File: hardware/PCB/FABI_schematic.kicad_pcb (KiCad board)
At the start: 2 copper layers, 78 x 55 mm, 37 parts, among them J1 Cliff_68125, J10 Conn_01x03_Male, J11 Conn_01x04_Male, J11_disp1 Conn_01x04_Female, J2 Cliff_68125, J3 Cliff_68125, J4 Cliff_68125, J5 Cliff_68125, J6 Cliff_68125, J7 Cliff_68125, J8 Cliff_68125, J9 Conn_02x05_Odd_Even, U1 MPXV7007GP, U2 ProMicro

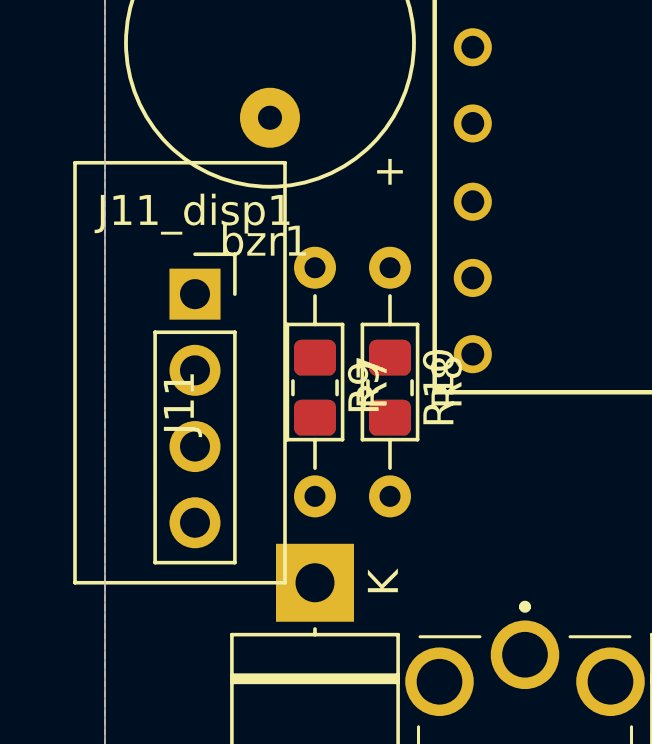
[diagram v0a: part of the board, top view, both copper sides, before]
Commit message: Pins changed and connected to AddOn
Signed-off-by: fussthalerandreas <fussthaler.andreas1997@gmail.com>
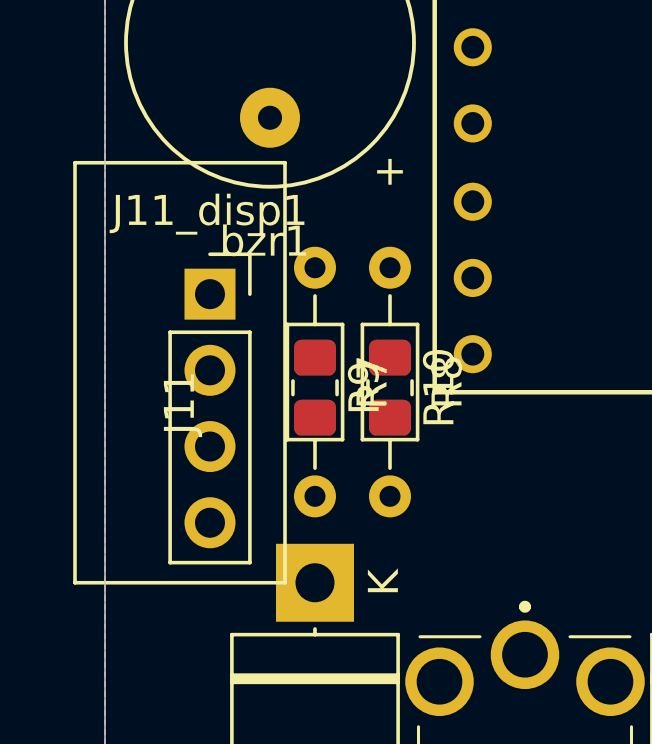
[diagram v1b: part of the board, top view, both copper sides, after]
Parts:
- moved J11_disp1 0.50 mm to (76.5, 124.4)

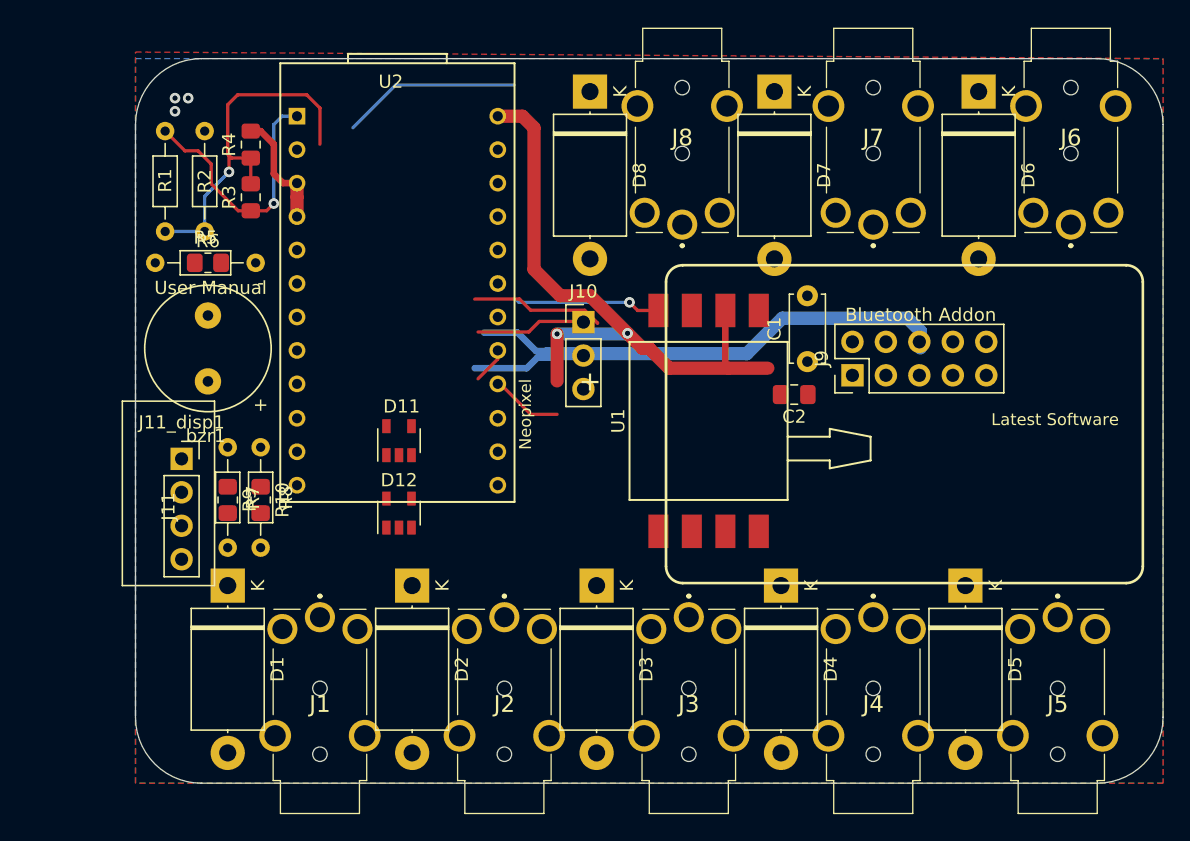
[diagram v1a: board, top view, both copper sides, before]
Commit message: Display positioning: adding adapted PinSocket to enable soldering and pluggin in of the display, 3D Models adapted
Signed-off-by: fussthalerandreas <fussthaler.andreas1997@gmail.com>
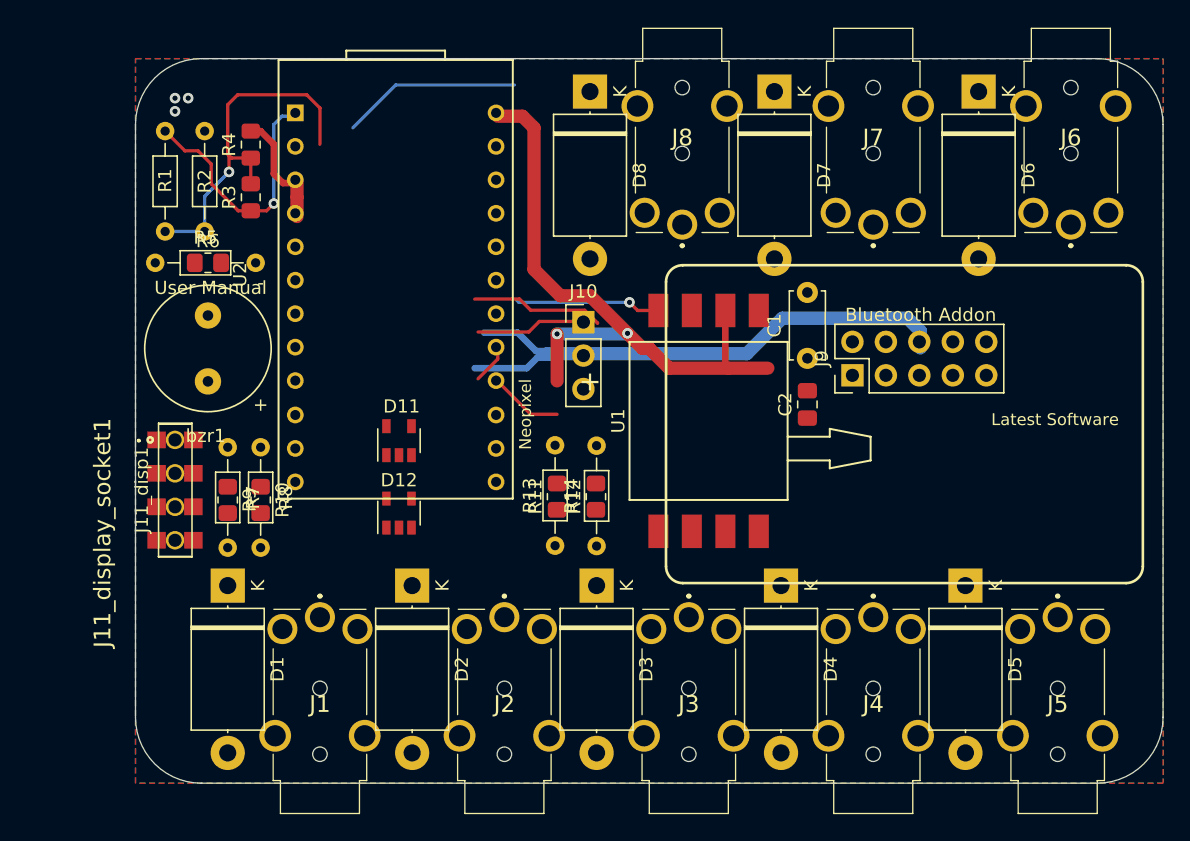
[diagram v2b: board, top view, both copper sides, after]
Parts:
- removed J11: Conn_01x04_Male, Connector:display
- added J11_display_socket1: 91601-304LF, SamacSys_Parts:91601304LF, F.Cu at (76.0, 126.8)
- added R11: 10k, Resistor_SMD:R_0805_2012Metric_Pad1.20x1.40mm_HandSolder, F.Cu at (105.0, 127.2)
- added R12: 18k, Resistor_SMD:R_0805_2012Metric_Pad1.20x1.40mm_HandSolder, F.Cu at (108.0, 127.2)
- added R13: 10k, Resistor_THT:R_Axial_DIN0204_L3.6mm_D1.6mm_P7.62mm_Horizontal, F.Cu at (104.8, 131.0)
- added R14: 18k, Resistor_THT:R_Axial_DIN0204_L3.6mm_D1.6mm_P7.62mm_Horizontal, F.Cu at (108.0, 131.0)
- J11_disp1: footprint Connector_PinSocket_2.54mm:PinSocket_1x04_P2.54mm_Vertical -> FABI_customLibs:OLED_display_091
- moved J11_disp1 2.95 mm to (74.8, 126.8), turned to 90 degrees
- moved C2 1.25 mm to (124.0, 120.2), turned to 90 degrees
- moved U2 0.28 mm to (92.8, 110.8)
- moved C1 0.25 mm to (124.0, 116.8)
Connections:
- net buzzer_pin renamed Buzzer_Pin
- J9 pad 1: AddOn_Pin1 -> ESP_AddOn_Pin1
- J9 pad 9: VCC -> VDD
- U2 pad 21: (no net) -> VCC
- U2 pad 24: VCC -> VDD
- U2 pad 5: SCL -> SDA
- U2 pad 6: SDA -> SCL

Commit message: Signed-off-by: fussthalerandreas <fussthaler.andreas1997@gmail.com>
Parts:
- removed J11_display_socket1: 91601-304LF, SamacSys_Parts:91601304LF
- added J11: dispaly_connector_91601-304LF, FABI_customLibs:91601304LF, F.Cu at (76.5, 126.2)
- moved R9 2.66 mm to (81.8, 125.5), turned to 0 degrees
- moved R7 0.90 mm to (80.5, 122.8)
- moved R8 0.79 mm to (82.8, 122.8)
- moved R10 0.75 mm to (81.8, 127.5), turned to 0 degrees
- moved J11_disp1 0.56 mm to (75.0, 126.2)
- moved D12 0.40 mm to (93.0, 128.9)
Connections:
- J1 pad 2R: (no net) -> Net-(J1-Pad2R)
- J1 pad 6SR: (no net) -> Net-(J1-Pad6SR)
- J2 pad 2R: (no net) -> Net-(J2-Pad2R)
- J2 pad 6SR: (no net) -> Net-(J2-Pad6SR)
- J3 pad 2R: (no net) -> Net-(J3-Pad2R)
- J3 pad 6SR: (no net) -> Net-(J3-Pad6SR)
- J4 pad 2R: (no net) -> Net-(J4-Pad2R)
- J4 pad 6SR: (no net) -> Net-(J4-Pad6SR)
- J5 pad 2R: (no net) -> Net-(J5-Pad2R)
- J5 pad 6SR: (no net) -> Net-(J5-Pad6SR)
- J6 pad 2R: (no net) -> Net-(J6-Pad2R)
- J6 pad 6SR: (no net) -> Net-(J6-Pad6SR)
- J7 pad 2R: (no net) -> Net-(J7-Pad2R)
- J7 pad 6SR: (no net) -> Net-(J7-Pad6SR)
- J8 pad 2R: (no net) -> Net-(J8-Pad2R)
- J8 pad 6SR: (no net) -> Net-(J8-Pad6SR)
- J9 pad 4: (no net) -> Net-(J9-Pad4)
- J9 pad 5: (no net) -> Net-(J9-Pad5)
- U1 pad 1: (no net) -> Net-(U1-Pad1)
- U1 pad 5: (no net) -> Net-(U1-Pad5)
- U1 pad 6: (no net) -> Net-(U1-Pad6)
- U1 pad 7: (no net) -> Net-(U1-Pad7)
- U1 pad 8: (no net) -> Net-(U1-Pad8)
- U2 pad 22: (no net) -> Net-(U2-Pad22)
- U2 pad 23: (no net) -> Net-(U2-Pad23)
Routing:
- net 5: track 0.00 -> 19.7 mm
- net 4: track 0.00 -> 19.7 mm
- net 3: track 0.00 -> 19.7 mm
- net 2: track 0.00 -> 19.7 mm
- net SDA: track 0.00 -> 17.4 mm
- net 1: track 0.00 -> 11.9 mm
- net SCL: track 0.00 -> 7.61 mm
- net Net-(R5-Pad2): track 0.00 -> 7.03 mm

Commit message: routed the PCB, adapted all components, ready for review
Signed-off-by: fussthalerandreas <fussthaler.andreas1997@gmail.com>
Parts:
- added REF**: ESP32_Addon, FABI_customLibs:ESP32_Addon, F.Cu at (132.5, 116.8)
- R3, R4: footprint Resistor_SMD:R_0805_2012Metric_Pad1.15x1.40mm_HandSolder -> Resistor_SMD:R_0805_2012Metric_Pad1.20x1.40mm_HandSolder
- U1: footprint MPXV7007:MPXV7007GP -> MPXV7007GP:MPXV7007GP
- moved R5 9.50 mm to (74.8, 119.0)
- moved R6 9.50 mm to (78.5, 119.0)
- moved R13 8.30 mm to (102.9, 122.9), turned to 0 degrees
- moved R14 7.50 mm to (102.9, 125.5), turned to 0 degrees
- moved D11 7.20 mm to (93.0, 130.2)
- moved D12 6.70 mm to (93.0, 122.2), turned to 0 degrees
- moved R4 5.13 mm to (78.5, 104.5), turned to 180 degrees
- moved R2 4.88 mm to (82.4, 104.5), turned to 180 degrees
- moved R11 4.67 mm to (106.7, 122.9), turned to 0 degrees
- moved bzr1 4.25 mm to (78.5, 111.8), turned to 0 degrees
- moved R3 3.97 mm to (78.5, 102.2), turned to 0 degrees
- moved R1 2.80 mm to (74.8, 102.2), turned to 0 degrees
- moved R7 2.25 mm to (82.8, 122.8)
- moved R12 2.15 mm to (106.7, 125.5), turned to 0 degrees
- moved R8 2.00 mm to (80.8, 122.8)
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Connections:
- U2 pad 10: 6 -> 3
- U2 pad 11: 1 -> 2
- U2 pad 12: 2 -> 1
- U2 pad 18: Buzzer_Pin -> 6
- U2 pad 7: 3 -> Buzzer_Pin
- U2 pad 8: 4 -> 5
- U2 pad 9: 5 -> 4
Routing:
- net 7: track 0.00 -> 69.3 mm, vias 0 -> 2
- net 6: track 13.8 -> 81.0 mm, vias 0 -> 1
- net 5: track 19.7 -> 79.4 mm
- net /A_RX: track 0.10 -> 58.8 mm, vias 0 -> 1
- net 8: track 0.00 -> 57.7 mm, vias 0 -> 2
- net VDD: track 0.00 -> 50.7 mm
- net 4: track 19.7 -> 64.1 mm
- net GND: track 52.2 -> 8.05 mm, vias 3 -> 0
- net VCC: track 56.2 -> 18.5 mm, vias 2 -> 0
- net /ESP_RX: track 37.8 -> 72.8 mm, vias 1 -> 2
- net AddOn_Pin3: track 0.00 -> 31.8 mm, vias 0 -> 1
- net 3: track 19.7 -> 50.8 mm
- net AddOn_Pin2: track 0.00 -> 29.0 mm
- net ESP_AddOn_Pin1: track 0.00 -> 28.2 mm
- net 1: track 11.9 -> 38.1 mm
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- added copper zone on B.Cu, net VCC
- removed copper zone on B.Cu, net GND

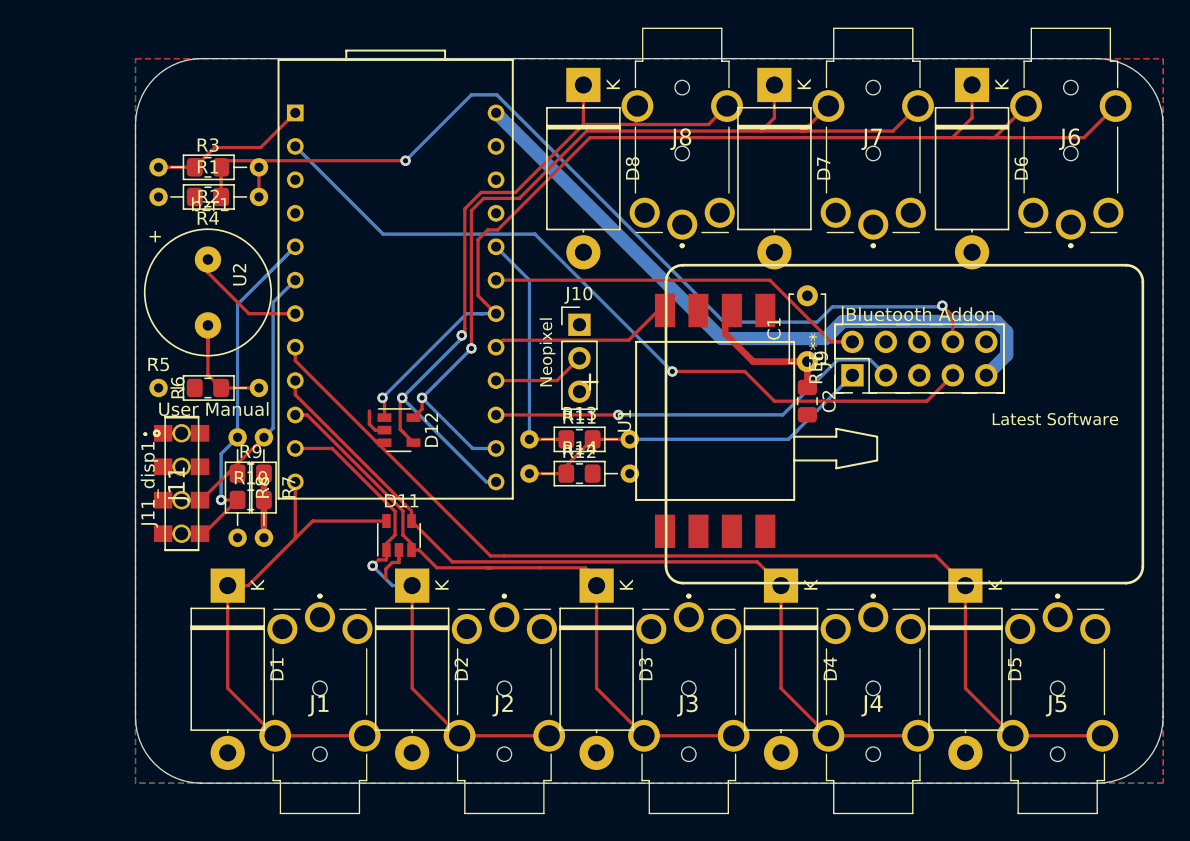
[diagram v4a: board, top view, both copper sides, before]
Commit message: PCB v2, after Feedback (according to Meeting 2)
Signed-off-by: fussthalerandreas <fussthaler.andreas1997@gmail.com>
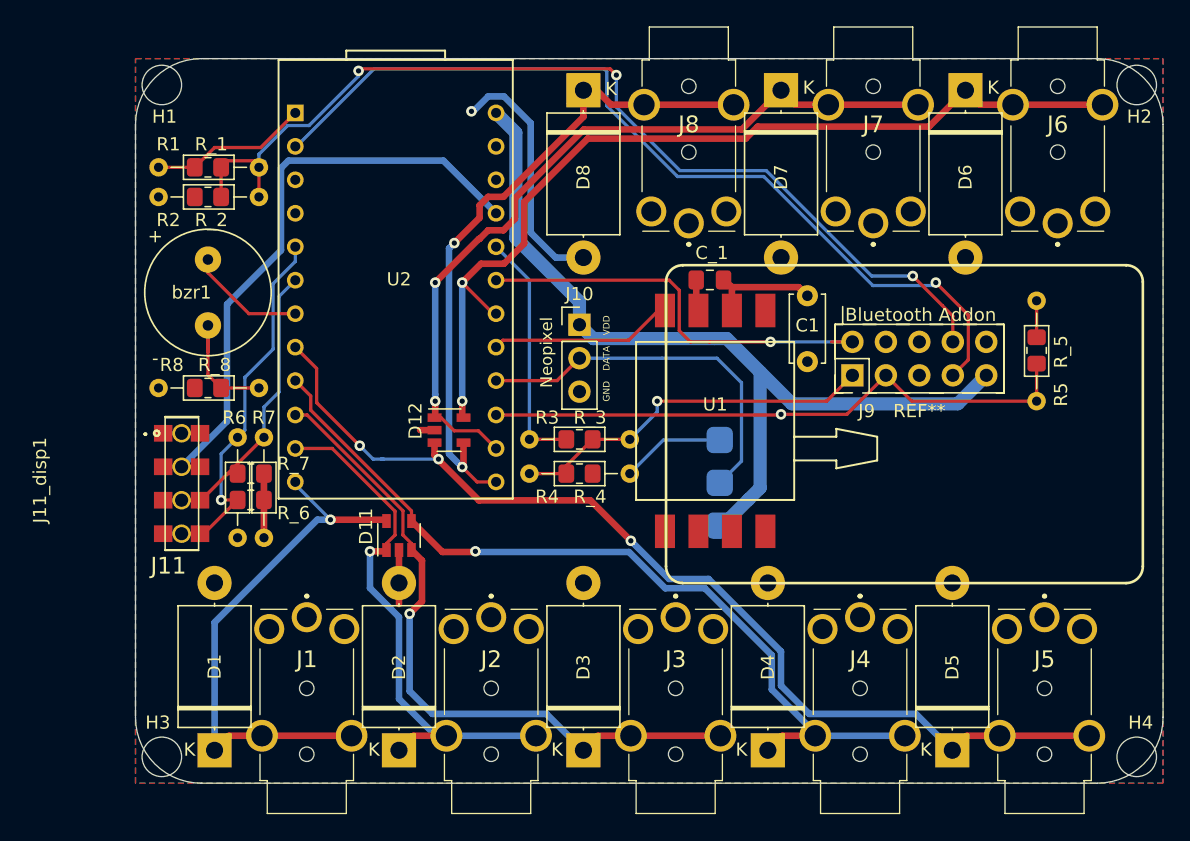
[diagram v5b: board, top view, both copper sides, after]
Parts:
- added DATA: SolderWirePad_1x01_SMD_1x2mm, Connector_Wire:SolderWirePad_1x01_SMD_1x2mm, B.Cu at (117.3, 126.2)
- added GND: SolderWirePad_1x01_SMD_1x2mm, Connector_Wire:SolderWirePad_1x01_SMD_1x2mm, B.Cu at (117.3, 123.0)
- added H1: MountingHole, MountingHole:MountingHole_3mm, F.Cu at (75.0, 96.0)
- added H2: MountingHole, MountingHole:MountingHole_3mm, F.Cu at (149.0, 96.0)
- added H3: MountingHole, MountingHole:MountingHole_3mm, F.Cu at (75.0, 147.0)
- added H4: MountingHole, MountingHole:MountingHole_3mm, F.Cu at (149.0, 147.0)
- added R5: 10k, Resistor_THT:R_Axial_DIN0204_L3.6mm_D1.6mm_P7.62mm_Horizontal, F.Cu at (141.4, 120.0)
- added R_5: 10k, Resistor_SMD:R_0805_2012Metric_Pad1.20x1.40mm_HandSolder, F.Cu at (141.4, 116.2)
- added VDD: SolderWirePad_1x01_SMD_1x2mm, Connector_Wire:SolderWirePad_1x01_SMD_1x2mm, B.Cu at (117.3, 129.4)
- moved D1 12.5 mm to (79.0, 146.5), turned to 90 degrees
- moved D2 12.5 mm to (93.0, 146.5), turned to 90 degrees
- moved D3 12.5 mm to (107.0, 146.5), turned to 90 degrees
- moved D4 12.5 mm to (121.0, 146.5), turned to 90 degrees
- moved D5 12.5 mm to (135.0, 146.5), turned to 90 degrees
- moved C_1 11.8 mm to (116.6, 110.8), turned to 180 degrees
- moved C1 5.00 mm to (124.0, 112.0), turned to 270 degrees
- moved D12 3.80 mm to (96.8, 122.2)
- moved J6 1.00 mm to (143.0, 99.9)
- moved J1 1.00 mm to (86.0, 143.0)
- moved J2 1.00 mm to (100.0, 143.0)
- moved J3 1.00 mm to (114.0, 143.0)
- moved J4 1.00 mm to (128.0, 143.0)
- moved J5 1.00 mm to (142.0, 143.0)
- moved D6 0.64 mm to (136.0, 96.4)
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- renumbered C2 to C_1, R13 to R3, R14 to R4, R8 to R6, R5 to R8, R3 to R_1, R4 to R_2, R11 to R_3, R12 to R_4, R10 to R_6, R9 to R_7, R6 to R_8
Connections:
- net /A_RX renamed A_RX
- net /A_TX renamed A_TX
- net /ESP_RX renamed ESP_RX
- net /MPX renamed MPX
- net /NEOPIXEL renamed NEOPIXEL
- net 1 renamed AUX_1
- net 2 renamed AUX_2
- net 3 renamed AUX_3
- net 4 renamed AUX_4
- net 5 renamed AUX_5
- net 8 renamed AUX_8
- D12 pad 1: 6 -> AUX_7
- D12 pad 5: 7 -> AUX_6
- D6 pad 1: 6 -> AUX_6
- D7 pad 1: 7 -> AUX_7
- J10 pad 1: VCC -> VDD
- J6 pad 3T: 6 -> AUX_6
- J7 pad 3T: 7 -> AUX_7
- U2 pad 14: 7 -> AUX_7
- U2 pad 18: 6 -> AUX_6
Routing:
- net 6: track 81.0 -> 0.00 mm, vias 1 -> 0
- net AUX_6: track 0.00 -> 71.2 mm, vias 0 -> 2
- net 7: track 69.3 -> 0.00 mm, vias 2 -> 0
- net AUX_7: track 0.00 -> 60.3 mm, vias 0 -> 2
- net VCC: track 18.5 -> 60.7 mm
- net GND: track 8.05 -> 44.2 mm, vias 0 -> 1
- net NEOPIXEL: track 7.03 -> 28.4 mm
- net VDD: track 50.7 -> 66.2 mm
- net AddOn_Pin3: track 31.8 -> 45.9 mm
- net A_RX: track 58.8 -> 68.1 mm
- net AUX_8: track 57.7 -> 50.9 mm
- net ESP_RX: track 72.8 -> 76.8 mm, vias 2 -> 3
- net AUX_2: track 38.1 -> 41.8 mm
- net AddOn_Pin2: track 29.0 -> 32.5 mm, vias 0 -> 1
- net SDA: track 33.2 -> 29.9 mm
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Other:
- board text added: "DATA"
- board text added: "GND"
- board text added: "VDD"
- board text removed: "+"
- board text removed: "Latest Software"
- board text removed: "Supported by:"
- board text removed: "User Manual"

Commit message: adapted PCB according to Feedback (mounting holes, ProMicro pins enlarged, TVS-diods and arrays repositioned and routes enlarged to 0.5mm, NeoPixel SMD Pads, +element labels)
Signed-off-by: fussthalerandreas <fussthaler.andreas1997@gmail.com>
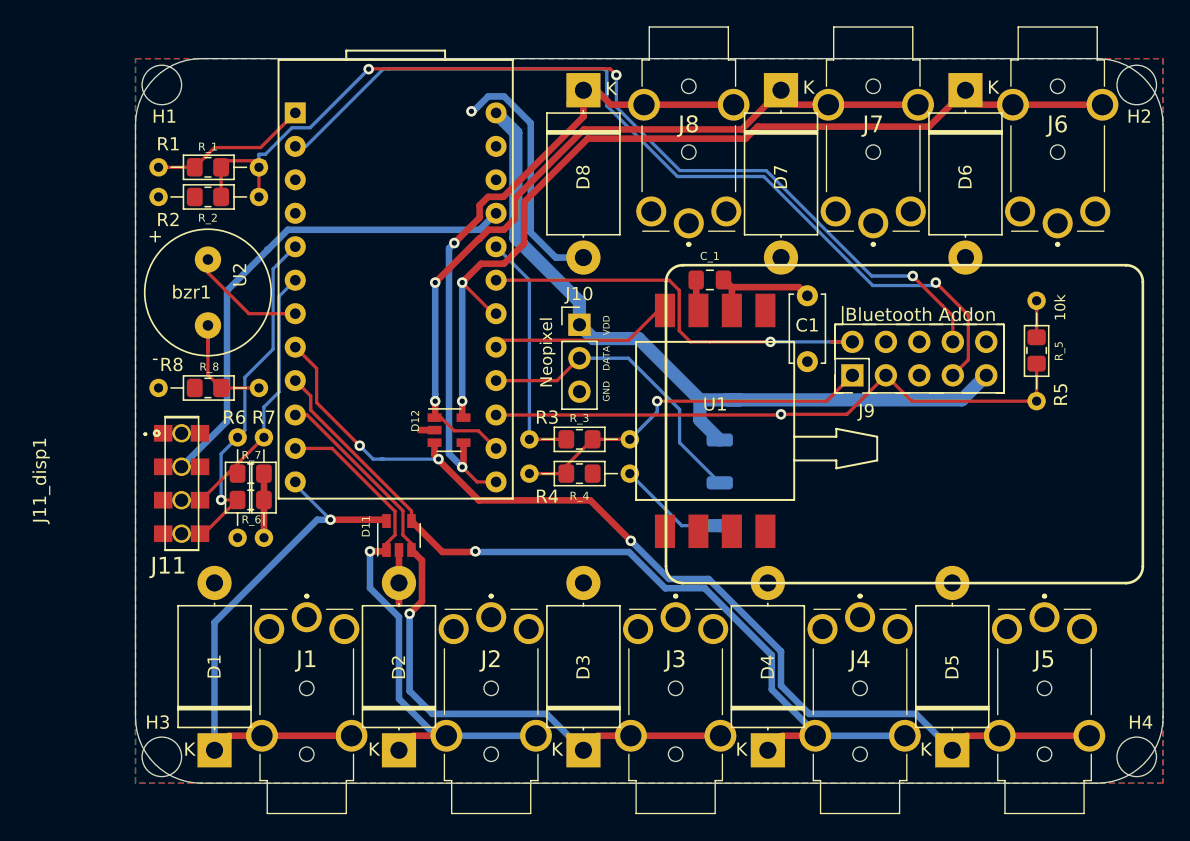
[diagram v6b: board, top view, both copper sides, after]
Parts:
- U2: footprint ProMicro:ProMicro -> FABI_customLibs:ProMicro
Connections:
- GND pad 1: GND -> VDD
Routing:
- net VDD: track 66.2 -> 57.5 mm
- net VCC: track 60.7 -> 54.5 mm
- net NEOPIXEL: track 28.4 -> 23.1 mm
- net GND: track 44.2 -> 45.0 mm
